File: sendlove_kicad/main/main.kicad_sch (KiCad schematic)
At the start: 20 parts, among them J1 USB-C 16P, J2 BATT, Q1 AO3401A, SW1 POWER, U1 USBLC6-2SC6, U2 TP4056-42-ESOP8, U3 RT9080-33GJ5

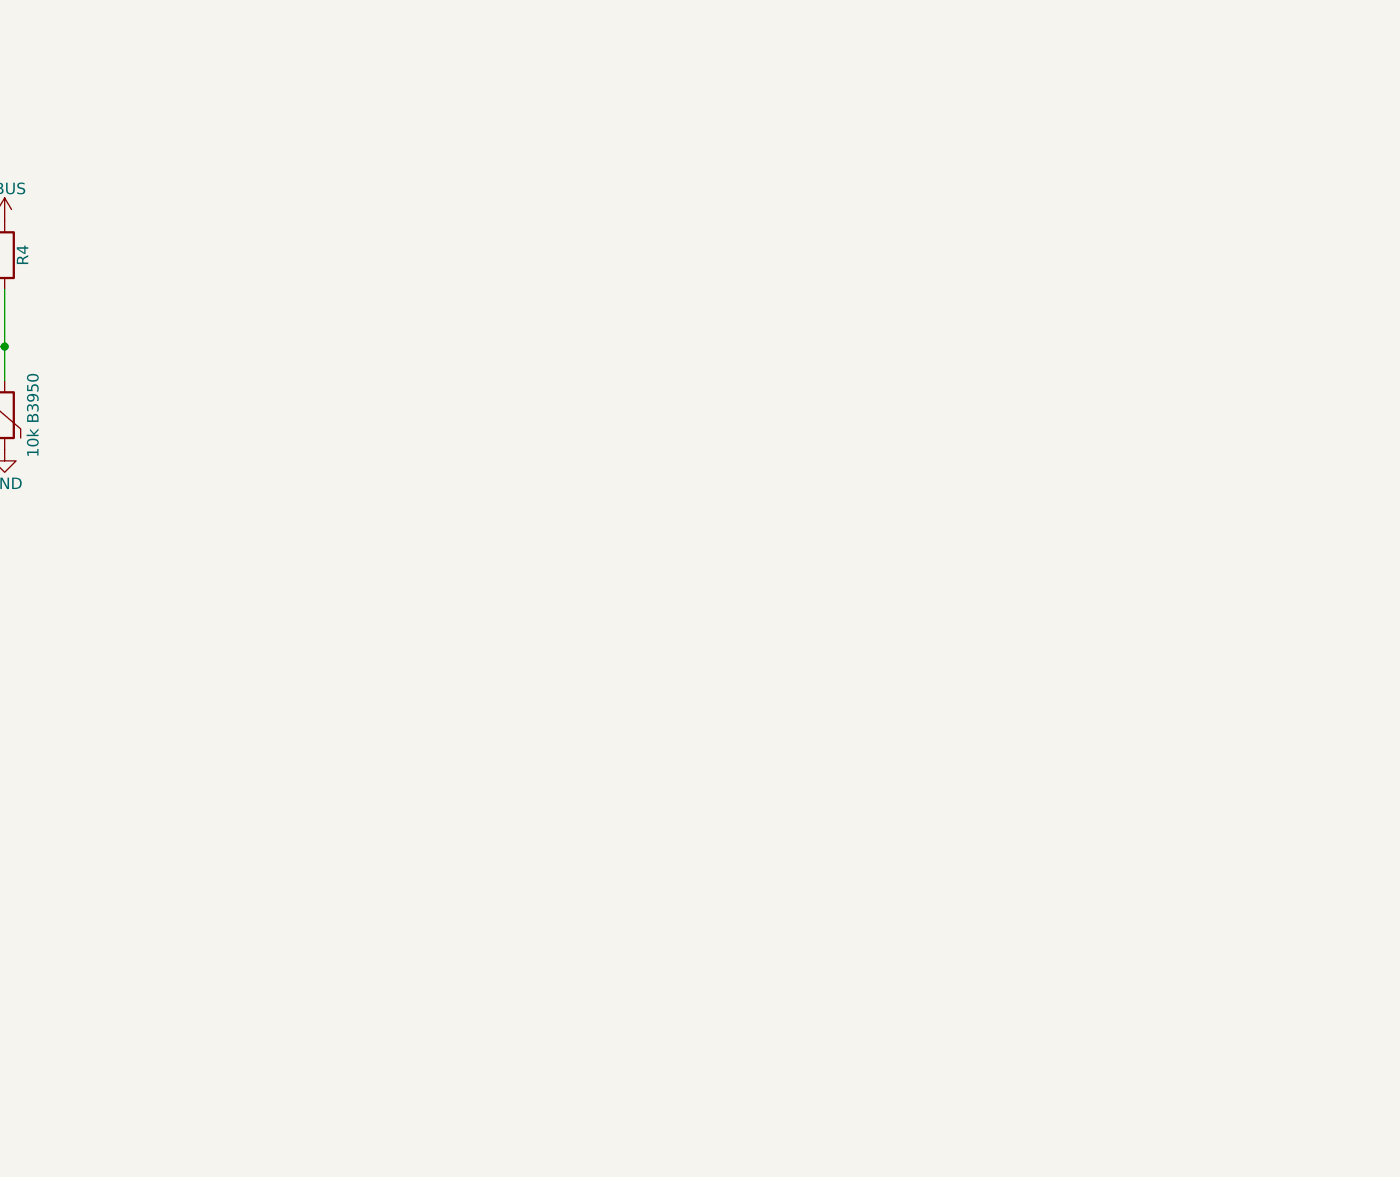
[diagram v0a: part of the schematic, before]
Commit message: refactor(hw): ve lai schematic - khoi ESP32-C3 (dang lam)
Co-Authored-By: Claude Opus 5.5 <noreply@anthropic.com>
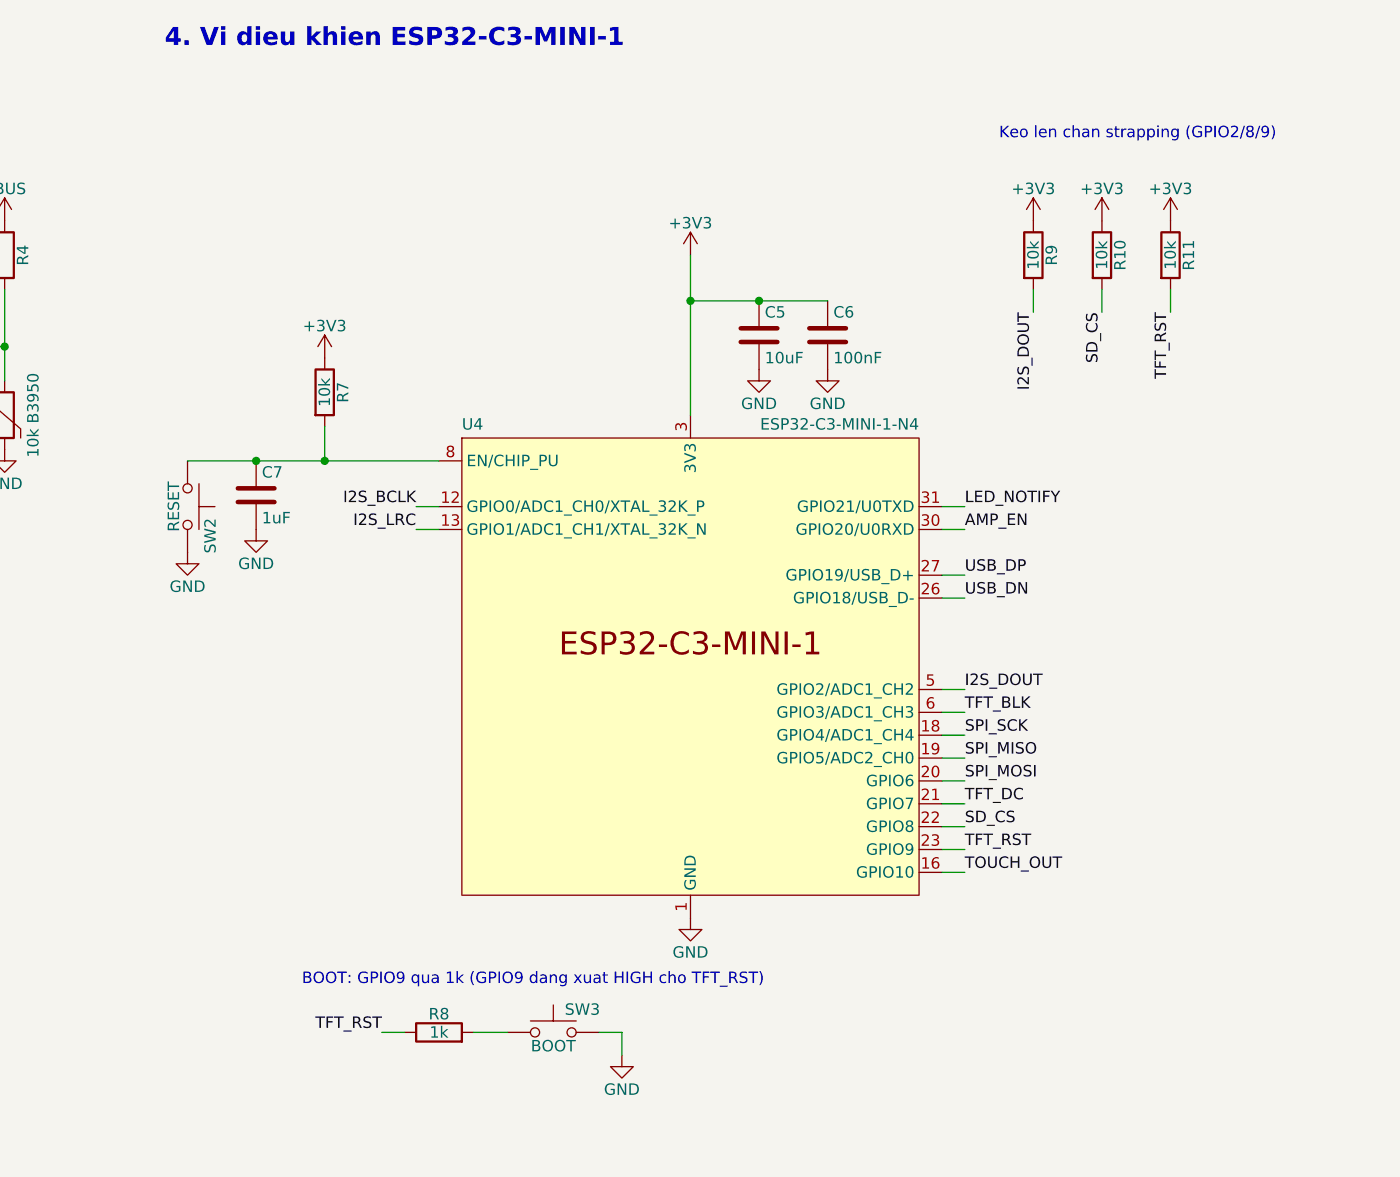
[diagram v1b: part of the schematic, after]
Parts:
- added C5: 10uF, Capacitor_SMD:C_0603_1608Metric, symbol Device:C
- added C6: 100nF, Capacitor_SMD:C_0402_1005Metric, symbol Device:C
- added C7: 1uF, Capacitor_SMD:C_0603_1608Metric, symbol Device:C
- added R10, R11, R7, R9: 10k, Resistor_SMD:R_0603_1608Metric, symbol Device:R
- added R8: 1k, Resistor_SMD:R_0603_1608Metric, symbol Device:R
- added SW2: RESET, Button_Switch_SMD:SW_SPST_PTS810, symbol Switch:SW_Push
- added SW3: BOOT, Button_Switch_SMD:SW_SPST_PTS810, symbol Switch:SW_Push
- added U4: ESP32-C3-MINI-1-N4, PCM_Espressif:ESP32-C3-MINI-1, symbol Espressif:ESP32-C3-MINI-1
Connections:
- net +3V3: now also C5.1, C6.1, R10.1, R11.1, R7.1, R9.1, U4.3 (3V3)
- net GND: now also C5.2, C6.2, C7.2, SW2.2, SW3.2, U4.1 (GND), U4.11 (GND), U4.14 (GND), U4.2 (GND), U4.36 (GND), U4.37 (GND), U4.38 (GND), U4.39 (GND), U4.40 (GND), U4.41 (GND), U4.42 (GND), U4.43 (GND), U4.44 (GND), U4.45 (GND), U4.46 (GND), U4.47 (GND), U4.48 (GND), U4.49 (GND), U4.50 (GND), U4.51 (GND), U4.52 (GND), U4.53 (GND)
- net USB_DN: now also U4.26 (GPIO18/USB_D-)
- net USB_DP: now also U4.27 (GPIO19/USB_D+)
- new net: R8.2, SW3.1
- new net: C7.1, R7.2, SW2.1, U4.8 (EN/CHIP_PU)
- new net AMP_EN: U4.30 (GPIO20/U0RXD)
- new net I2S_BCLK: U4.12 (GPIO0/ADC1_CH0/XTAL_32K_P)
- new net I2S_DOUT: R9.2, U4.5 (GPIO2/ADC1_CH2)
- new net I2S_LRC: U4.13 (GPIO1/ADC1_CH1/XTAL_32K_N)
- new net LED_NOTIFY: U4.31 (GPIO21/U0TXD)
- new net SD_CS: R10.2, U4.22 (GPIO8)
- new net SPI_MISO: U4.19 (GPIO5/ADC2_CH0)
- new net SPI_MOSI: U4.20 (GPIO6)
- new net SPI_SCK: U4.18 (GPIO4/ADC1_CH4)
- new net TFT_BLK: U4.6 (GPIO3/ADC1_CH3)
- new net TFT_DC: U4.21 (GPIO7)
- new net TFT_RST: R11.2, R8.1, U4.23 (GPIO9)
- new net TOUCH_OUT: U4.16 (GPIO10)
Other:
- note added: "4. Vi dieu khien ESP32-C3-MINI-1"
- note added: "BOOT: GPIO9 qua 1k (GPIO9 dang xuat HIGH cho TFT_RST)"
- note added: "Keo len chan strapping (GPIO2/8/9)"

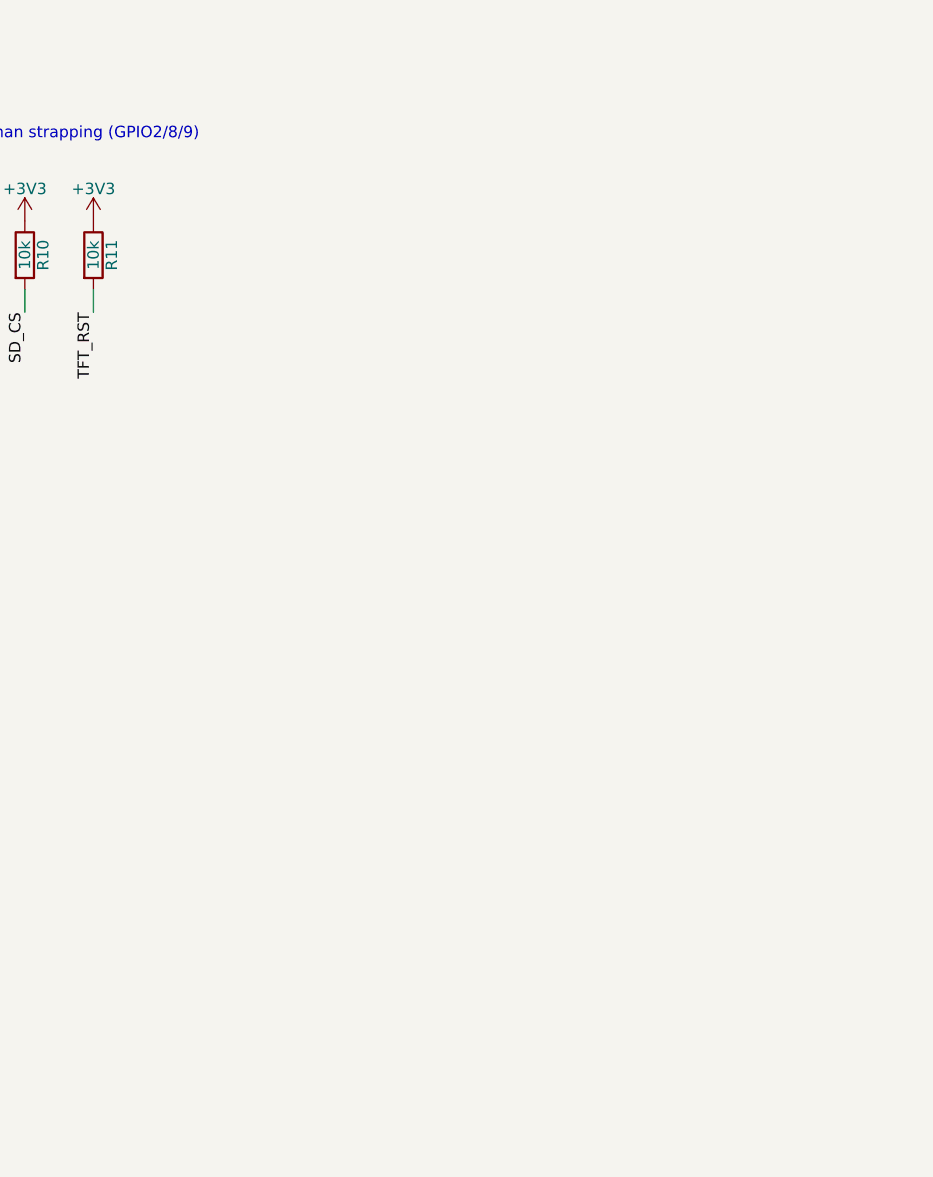
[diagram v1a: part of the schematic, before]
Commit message: refactor(hw): ve lai schematic - khoi man hinh + microSD (dang lam)
Co-Authored-By: Claude Opus 5.5 <noreply@anthropic.com>
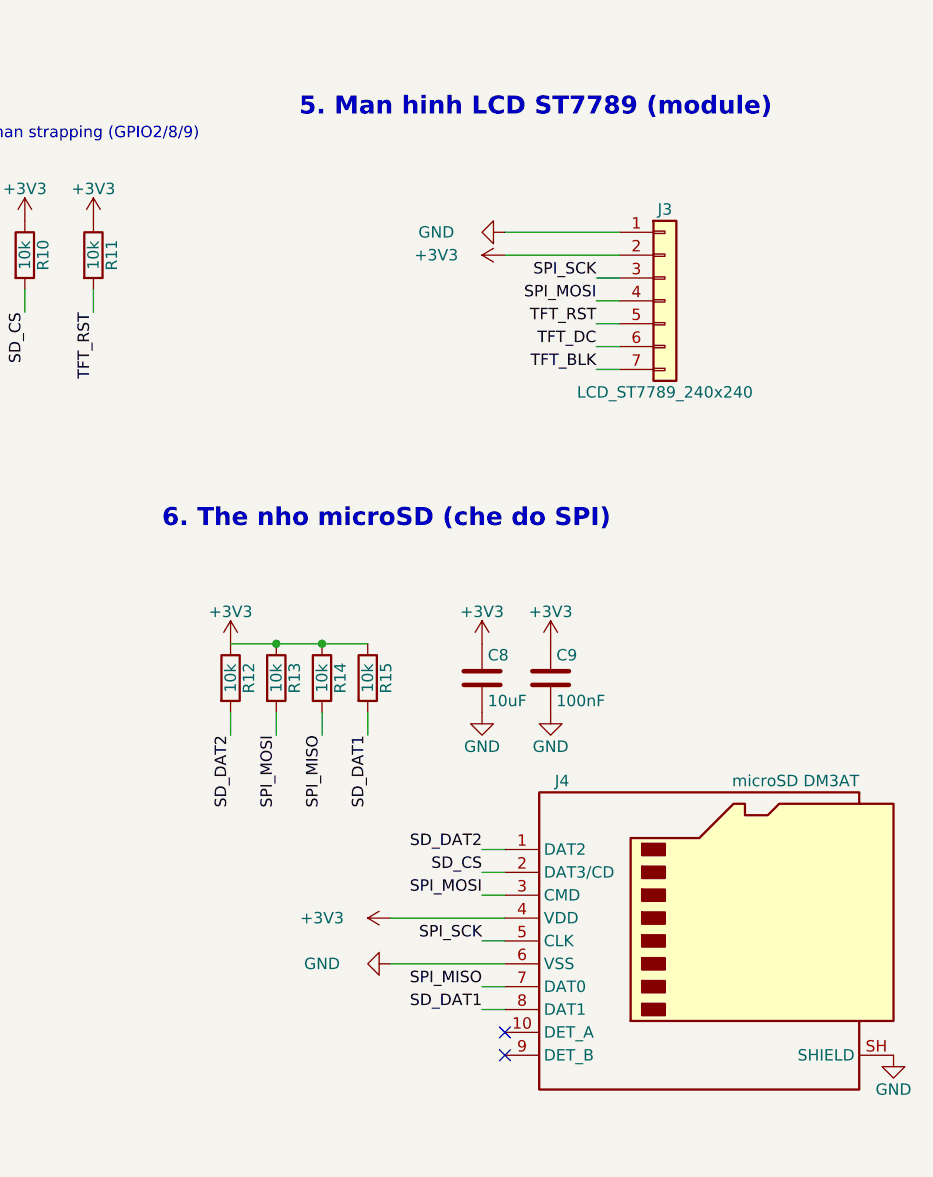
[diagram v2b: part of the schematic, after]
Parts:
- added C8: 10uF, Capacitor_SMD:C_0603_1608Metric, symbol Device:C
- added C9: 100nF, Capacitor_SMD:C_0402_1005Metric, symbol Device:C
- added J3: LCD_ST7789_240x240, Connector_PinHeader_2.54mm:PinHeader_1x07_P2.54mm_Vertical, symbol Connector_Generic:Conn_01x07
- added J4: microSD DM3AT, Connector_Card:microSD_HC_Hirose_DM3AT-SF-PEJM5, symbol Connector:Micro_SD_Card_Det_Hirose_DM3AT
- added R12, R13, R14, R15: 10k, Resistor_SMD:R_0603_1608Metric, symbol Device:R
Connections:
- net +3V3: now also C8.1, C9.1, J3.2 (Pin_2), J4.4 (VDD), R12.1, R13.1, R14.1, R15.1
- net GND: now also C8.2, C9.2, J3.1 (Pin_1), J4.6 (VSS), J4.SH (SHIELD)
- net SD_CS: now also J4.2 (DAT3/CD)
- net SPI_MISO: now also J4.7 (DAT0), R14.2
- net SPI_MOSI: now also J3.4 (Pin_4), J4.3 (CMD), R13.2
- net SPI_SCK: now also J3.3 (Pin_3), J4.5 (CLK)
- net TFT_BLK: now also J3.7 (Pin_7)
- net TFT_DC: now also J3.6 (Pin_6)
- net TFT_RST: now also J3.5 (Pin_5)
- new net SD_DAT1: J4.8 (DAT1), R15.2
- new net SD_DAT2: J4.1 (DAT2), R12.2
- no-connect marks 5 -> 7
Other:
- note added: "5. Man hinh LCD ST7789 (module)"
- note added: "6. The nho microSD (che do SPI)"

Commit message: refactor(hw): ve lai schematic - khoi am thanh, cam ung, LED (con 1 cho lech net USB)
Da du 9 khoi. ERC 0 loi. So netlist voi ban cu (b7ea78a): khop tru USB_DN/USB_DP,
phia dau noi (J1, U1 chan 1/3) va phia MCU (U1 chan 4/6, U4) dang la 2 net rieng,
ban cu la 1 net. Can noi lai truoc khi coi la xong.

Co-Authored-By: Claude Opus 5.5 <noreply@anthropic.com>
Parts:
- added C10: 10uF, Capacitor_SMD:C_0805_2012Metric, symbol Device:C
- added C11, C13: 100nF, Capacitor_SMD:C_0402_1005Metric, symbol Device:C
- added C12: 10pF (0-50pF), Capacitor_SMD:C_0603_1608Metric, symbol Device:C
- added D3: LED_NOTIFY, LED_SMD:LED_0603_1608Metric, symbol Device:LED
- added J5: SPEAKER 8R 1W, Connector_JST:JST_PH_S2B-PH-SM4-TB_1x02-1MP_P2.00mm_Horizontal, symbol Connector_Generic:Conn_01x02
- added R16: 680k, Resistor_SMD:R_0603_1608Metric, symbol Device:R
- added R17: 1k, Resistor_SMD:R_0603_1608Metric, symbol Device:R
- added TP1: TOUCH_PAD, TestPoint:TestPoint_Pad_D4.0mm, symbol Connector:TestPoint
- added U5: MAX98357AETE+, Package_DFN_QFN:TQFN-16-1EP_3x3mm_P0.5mm_EP1.23x1.23mm, symbol Audio:MAX98357A
- added U6: TTP223-BA6, Package_TO_SOT_SMD:SOT-23-6, symbol SendLove:TTP223-BA6
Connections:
- net +3V3: now also C13.1, U6.5 (VDD)
- net AMP_EN: now also R16.1
- net GND: now also C10.2, C11.2, C12.2, C13.2, D3.1 (K), U5.11 (GND), U5.15 (GND), U5.17 (PAD), U5.3 (GND), U6.2 (VSS), U6.4 (AHLB), U6.6 (TOG)
- net I2S_BCLK: now also U5.16 (BCLK)
- net I2S_DOUT: now also U5.1 (DIN)
- net I2S_LRC: now also U5.14 (LRCLK)
- net LED_NOTIFY: now also R17.1
- net TOUCH_OUT: now also U6.1 (Q)
- net VSYS: now also C10.1, C11.1, U5.7 (VDD), U5.8 (VDD)
- new net: D3.2 (A), R17.2
- new net: J5.2 (Pin_2), U5.10 (OUTN)
- new net: R16.2, U5.4 (~{SD_MODE})
- new net: J5.1 (Pin_1), U5.9 (OUTP)
- new net: C12.1, TP1.1, U6.3 (I)
- no-connect marks 7 -> 8
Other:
- note added: "7. Am thanh MAX98357A (VDD = VSYS)"
- note added: "8. Cam ung TTP223 (active HIGH, direct)"
- note added: "9. LED thong bao"

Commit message: refactor(hw): ve lai schematic xong - noi lai net USB, don chu cuoi
- Gan nhan USB_DN/USB_DP len day phia cong USB: truoc do phia dau noi va phia
  ESP32 cua USBLC6 la 2 net rieng (chi thong qua ben trong chip).
- Doi chu gia tri C12 khoi chu GND.
Kiem tra: netlist khop hoan toan voi ban truoc khi ve lai (b7ea78a, 36 net,
so theo nhom chan noi chung), ERC 0 loi (1 canh bao co y: EP MAX98357A noi
GND), khong net mot chan, khong chan bo sot.

Co-Authored-By: Claude Opus 5.5 <noreply@anthropic.com>
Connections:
- net USB_DN: now also J1.A7 (D-), J1.B7 (D-), U1.1 (I/O1)
- net USB_DP: now also J1.A6 (D+), J1.B6 (D+), U1.3 (I/O2)
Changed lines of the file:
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@@
 		)
 	)
+	(text "7. Am thanh MAX98357A (VDD = VSYS)"
+		(at 15.24 167.64 0)
+		(effects
+			(font
+				(size 2 2)
+				(bold yes)
+			)
+			(justify left bottom)
+		)
+	)
+	(text "8. Cam ung TTP223 (active HIGH, direct)"
+		(at 140.97 167.64 0)
+		(effects
+			(font
+				(size 2 2)
+				(bold yes)
+			)
+			(justify left bottom)
+		)
+	)
+	(text "9. LED thong bao"
+		(at 226.06 167.64 0)
+		(effects
+			(font
+				(size 2 2)
+				(bold yes)
+			)
+			(justify left bottom)
+		)
+	)
 	(label "USB_DN"
 		(at 86.36 50.8 0)
@@
 		)
 	)
-  (text "7. Am thanh MAX98357A (VDD = VSYS)"
-    (at 15.24 167.64 0)
-    (effects (font (size 2 2) (bold yes)) (justify left bottom))
-  )
-  (text "8. Cam ung TTP223 (active HIGH, direct)"
-    (at 140.97 167.64 0)
-    (effects (font (size 2 2) (bold yes)) (justify left bottom))
-  )
-  (text "9. LED thong bao"
-    (at 226.06 167.64 0)
-    (effects (font (size 2 2) (bold yes)) (justify left bottom))
-  )
+	(label "USB_DN"
+		(at 58.42 48.26 0)
+		(effects
+			(font
+				(size 1.27 1.27)
+			)
+			(justify left bottom)
+		)
+	)
+	(label "USB_DP"
+		(at 58.42 53.34 0)
+		(effects
+			(font
+				(size 1.27 1.27)
+			)
+			(justify left bottom)
+		)
+	)
 	(symbol
 		(lib_id "Connector:USB_C_Receptacle_USB2.0_16P")
@@
 		)
 		(property "Value" "10pF (0-50pF)"
-			(at 165.735 209.55 0)
+			(at 156.21 209.55 0)
 			(effects
 				(font
